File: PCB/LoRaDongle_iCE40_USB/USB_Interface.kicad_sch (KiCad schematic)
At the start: 28 parts, among them IC1 93LC56BT-I_OT, U2 FT232H, Y1 Crystal_GND24_Small

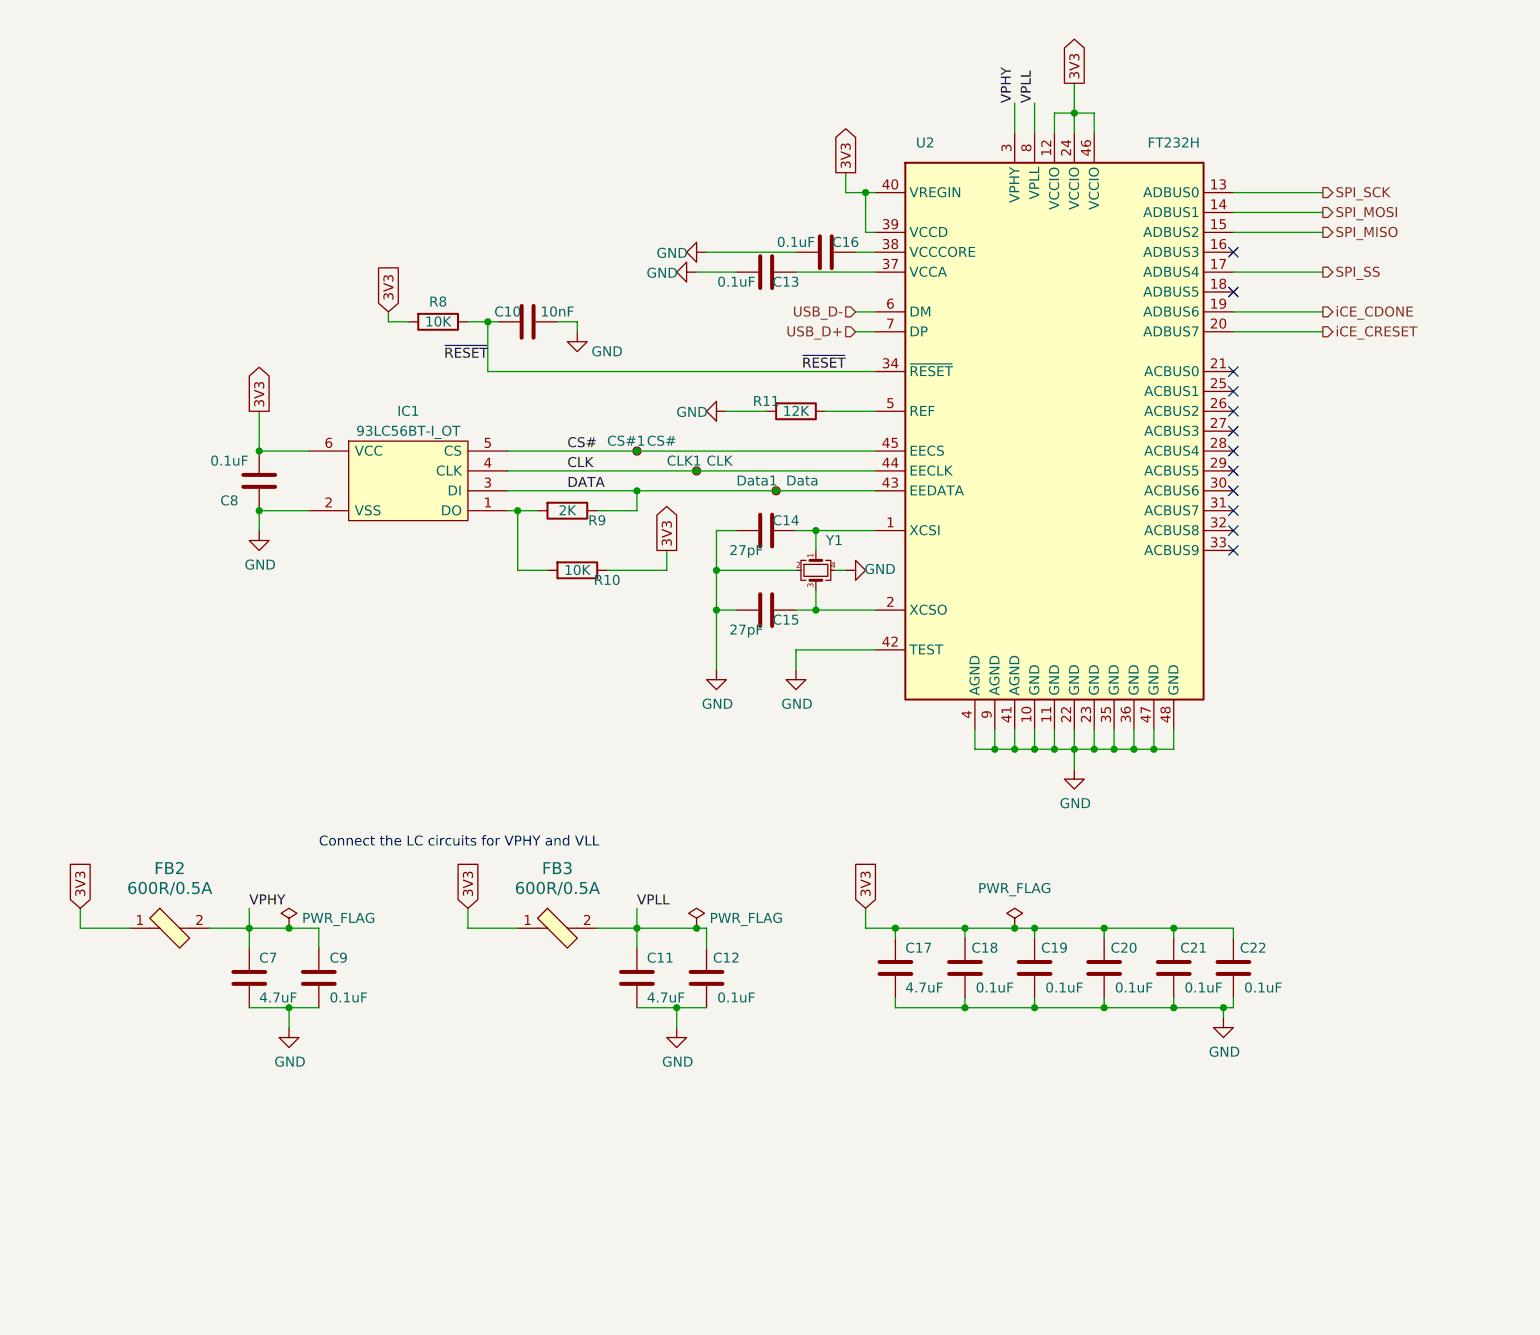
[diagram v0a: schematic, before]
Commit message: updated ftdi and flash chip, removed xilinx project
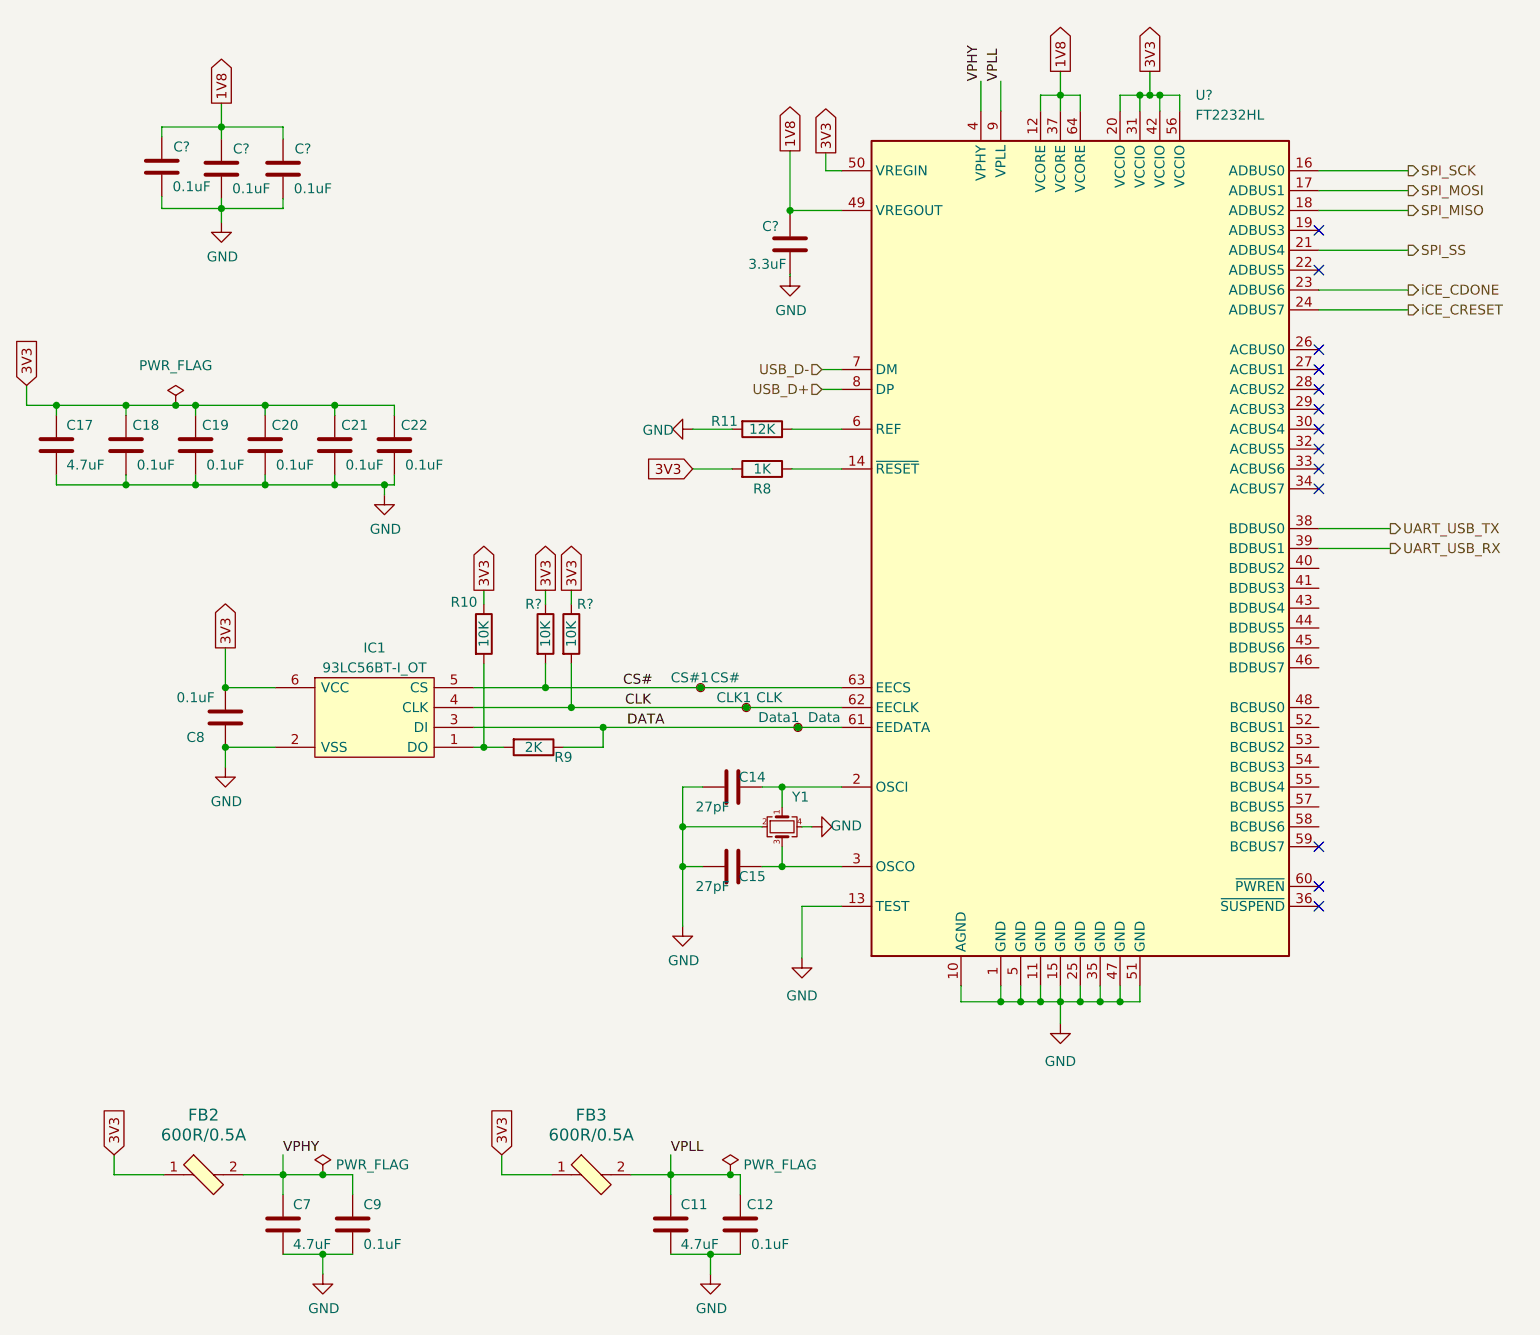
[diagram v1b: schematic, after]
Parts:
- removed C10: 10nF, Capacitor_SMD:C_0402_1005Metric_Pad0.74x0.62mm_HandSolder, symbol Device:C
- removed C13, C16: 0.1uF, Capacitor_SMD:C_0402_1005Metric_Pad0.74x0.62mm_HandSolder, symbol Device:C
- removed U2: FT232H, Package_QFP:LQFP-48_7x7mm_P0.5mm, symbol Interface_USB:FT232H
- added C? (x3): 0.1uF, Capacitor_SMD:C_0402_1005Metric_Pad0.74x0.62mm_HandSolder, symbol Device:C
- added C?: 3.3uF, symbol Device:C
- added R? (x2): 10K, Resistor_SMD:R_0402_1005Metric_Pad0.72x0.64mm_HandSolder, symbol Device:R
- added U?: FT2232HL, Package_QFP:LQFP-64_10x10mm_P0.5mm, symbol Interface_USB:FT2232HL
- R8: value 10K -> 1K; Manufacturer Part Number RMCF0402FT10K0 -> RMCF0402FT1K00
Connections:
- net 3V3: now also R?.1, R?.1, U?.20 (VCCIO), U?.31 (VCCIO), U?.42 (VCCIO), U?.50 (VREGIN), U?.56 (VCCIO)
- net CLK: now also R?.2, U?.62 (EECLK)
- net CS#: now also R?.2, U?.63 (EECS)
- net DATA: now also U?.61 (EEDATA)
- net GND: now also C?.1, C?.1, C?.1, C?.2, U?.1 (GND), U?.10 (AGND), U?.11 (GND), U?.13 (TEST), U?.15 (GND), U?.25 (GND), U?.35 (GND), U?.47 (GND), U?.5 (GND), U?.51 (GND)
- net SPI_MISO: now also U?.18 (ADBUS2)
- net SPI_MOSI: now also U?.17 (ADBUS1)
- net SPI_SCK: now also U?.16 (ADBUS0)
- net SPI_SS: now also U?.21 (ADBUS4)
- net USB_D+: now also U?.8 (DP)
- net USB_D-: now also U?.7 (DM)
- net VPHY: now also U?.4 (VPHY)
- net VPLL: now also U?.9 (VPLL)
- net iCE_CDONE: now also U?.23 (ADBUS6)
- net iCE_CRESET: now also U?.24 (ADBUS7)
- net at R11.1: now also U?.6 (REF)
- net at C14.1, Y1.1: now also U?.2 (OSCI)
- net at C15.1, Y1.3: now also U?.3 (OSCO)
- net ~{RESET}: no longer names the net of R8.1
- net ~{RESET}: now also U?.14 (~{RESET})
- new net 1V8: C?.1, C?.2, C?.2, C?.2, U?.12 (VCORE), U?.37 (VCORE), U?.49 (VREGOUT), U?.64 (VCORE)
- new net UART_USB_RX: U?.39 (BDBUS1)
- new net UART_USB_TX: U?.38 (BDBUS0)
- no-connect marks 12 -> 13
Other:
- note removed: "Connect the LC circuits for VPHY and VLL"
- moved on the sheet: C11, C12, C14, C15, C17, C18, C19, C20, C21, C22, C7, C8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

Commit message: updated jumpers, connectors and testpoints
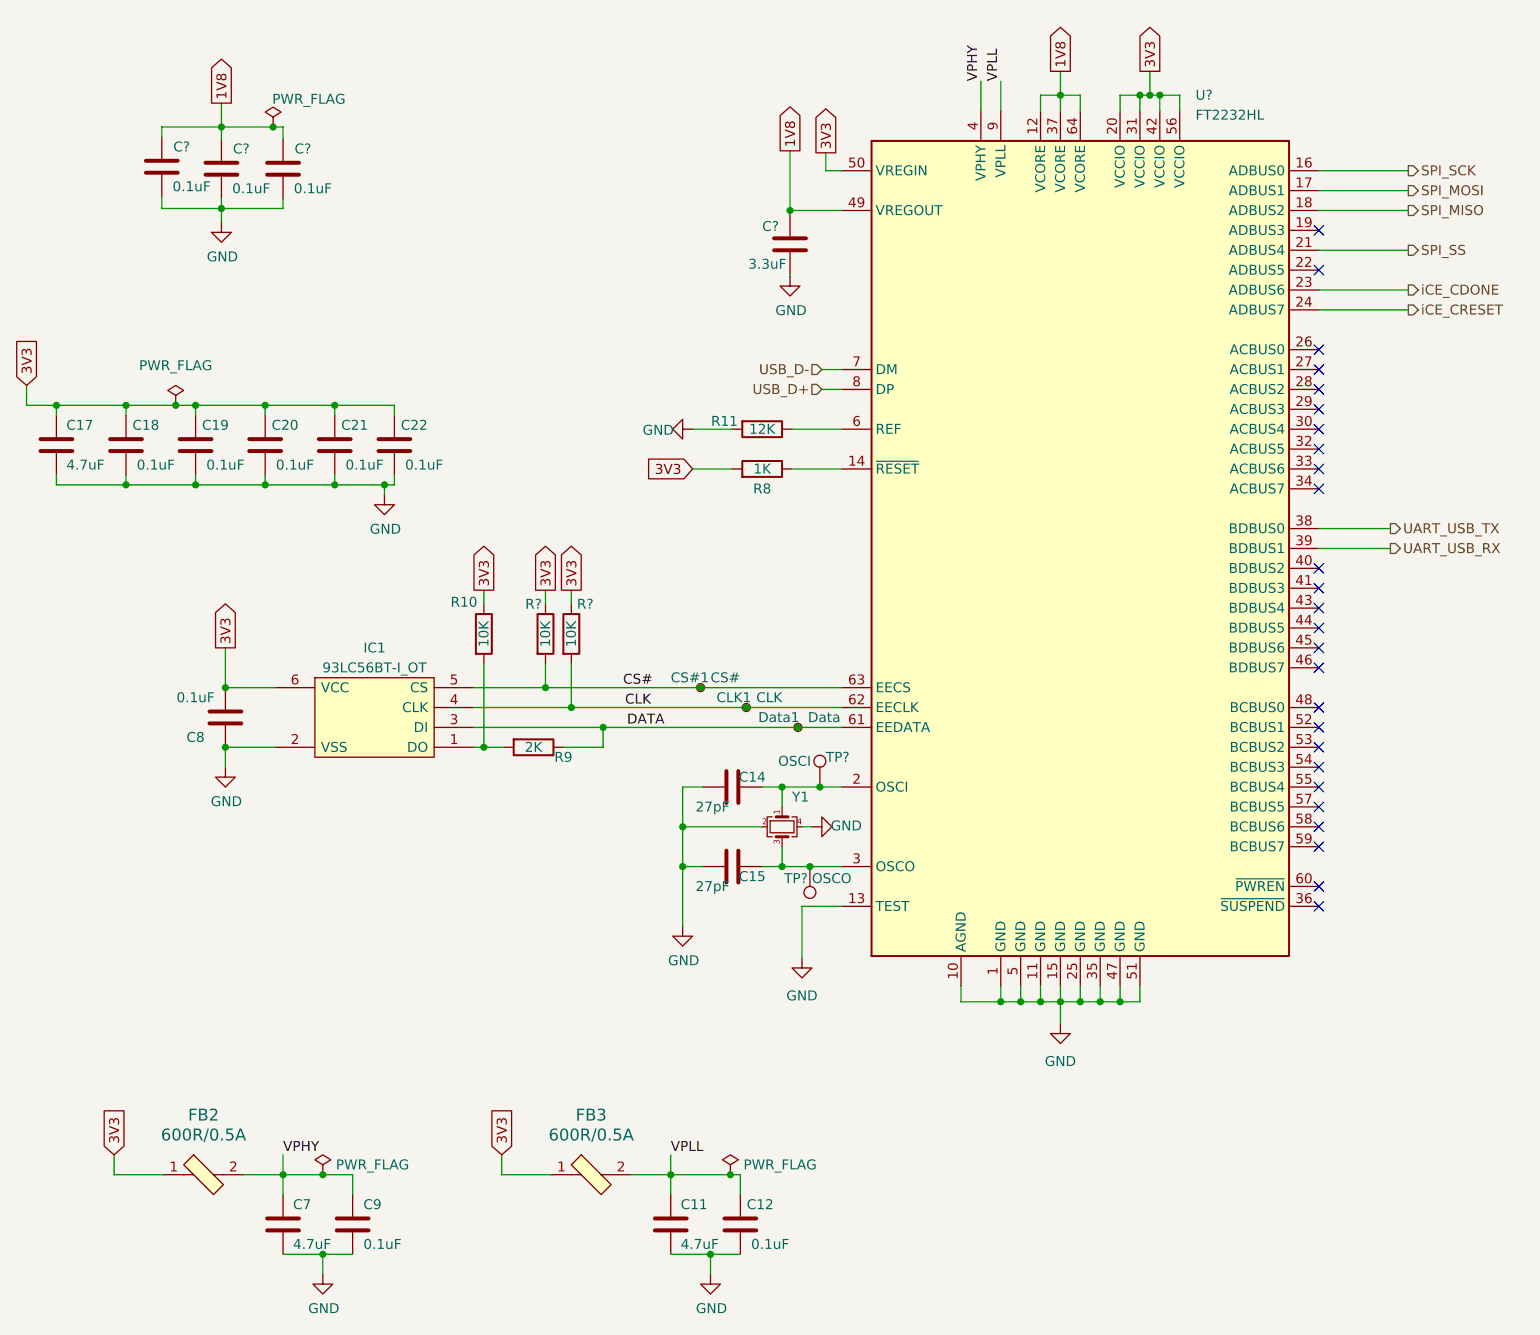
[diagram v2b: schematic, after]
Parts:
- added TP?: OSCO, symbol Connector:TestPoint
- added TP?: OSCI, symbol Connector:TestPoint
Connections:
- net at C15.1, U?.3 (OSCO), Y1.3: now also TP?.1
- net at C14.1, U?.2 (OSCI), Y1.1: now also TP?.1
- no-connect marks 13 -> 26
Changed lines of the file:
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@@
   (junction (at 54.102 67.818) (diameter 0) (color 0 0 0 0)
   )
+  (junction (at 66.548 32.258) (diameter 0) (color 0 0 0 0)
+  )
+  (junction (at 135.128 126.746) (diameter 0) (color 0 0 0 0)
+  )
   (junction (at 179.832 28.194) (diameter 0) (color 0 0 0 0)
   )
@@
   (junction (at 122.428 176.276) (diameter 0) (color 0 0 0 0)
   )
+  (junction (at 136.398 116.586) (diameter 0) (color 0 0 0 0)
+  )
   (junction (at 164.592 144.018) (diameter 0) (color 0 0 0 0)
   )
@@
   (junction (at 132.588 42.926) (diameter 0) (color 0 0 0 0)
   )
+  (no_connect (at 200.152 101.346))
+  (no_connect (at 200.152 114.046))
+  (no_connect (at 200.152 121.666))
   (no_connect (at 200.152 45.466))
+  (no_connect (at 200.152 106.426))
+  (no_connect (at 200.152 108.966))
+  (no_connect (at 200.152 98.806))
   (no_connect (at 200.152 131.826))
   (no_connect (at 200.152 129.286))
   (no_connect (at 200.152 124.206))
+  (no_connect (at 200.152 119.126))
   (no_connect (at 200.152 50.546))
   (no_connect (at 200.152 65.786))
@@
   (no_connect (at 200.152 70.866))
   (no_connect (at 200.152 78.486))
+  (no_connect (at 200.152 111.506))
+  (no_connect (at 200.152 116.586))
   (no_connect (at 200.152 60.706))
+  (no_connect (at 200.152 88.646))
+  (no_connect (at 200.152 91.186))
+  (no_connect (at 200.152 93.726))
+  (no_connect (at 200.152 96.266))
   (wire (pts (xy 74.422 77.978) (xy 80.772 77.978))
     (stroke (width 0) (type default) (color 0 0 0 0))
@@
     (stroke (width 0) (type default) (color 0 0 0 0))
   )
-  (wire (pts (xy 59.944 32.258) (xy 67.818 32.258))
+  (wire (pts (xy 59.944 32.258) (xy 66.548 32.258))
     (stroke (width 0) (type default) (color 0 0 0 0))
   )
@@
     (stroke (width 0) (type default) (color 0 0 0 0))
   )
-  (wire (pts (xy 139.192 126.746) (xy 131.572 126.746))
+  (wire (pts (xy 139.192 126.746) (xy 135.128 126.746))
     (stroke (width 0) (type default) (color 0 0 0 0))
   )
@@
     (stroke (width 0) (type default) (color 0 0 0 0))
   )
+  (wire (pts (xy 136.398 116.586) (xy 139.192 116.586))
+    (stroke (width 0) (type default) (color 0 0 0 0))
+  )
   (wire (pts (xy 169.672 28.194) (xy 169.672 30.226))
     (stroke (width 0) (type default) (color 0 0 0 0))
@@
     (stroke (width 0) (type default) (color 0 0 0 0))
   )
-  (wire (pts (xy 131.572 116.586) (xy 139.192 116.586))
+  (wire (pts (xy 131.572 116.586) (xy 136.398 116.586))
     (stroke (width 0) (type default) (color 0 0 0 0))
   )
@@
     (stroke (width 0) (type default) (color 0 0 0 0))
   )
+  (wire (pts (xy 66.548 32.258) (xy 67.818 32.258))
+    (stroke (width 0) (type default) (color 0 0 0 0))
+  )
   (wire (pts (xy 93.472 111.506) (xy 96.012 111.506))
     (stroke (width 0) (type default) (color 0 0 0 0))
@@
   )
   (wire (pts (xy 59.944 42.672) (xy 59.944 44.45))
+    (stroke (width 0) (type default) (color 0 0 0 0))
+  )
+  (wire (pts (xy 135.128 126.746) (xy 131.572 126.746))
     (stroke (width 0) (type default) (color 0 0 0 0))
   )
@@
   (symbol (lib_id "power:GND") (at 167.132 146.812 0) (unit 1)
     (in_bom yes) (on_board yes) (fields_autoplaced)
-    (property "Reference" "#PWR?" (id 0) (at 167.132 153.162 0)
+    (property "Reference" "#PWR0119" (id 0) (at 167.132 153.162 0)
       (effects (font (size 1.27 1.27)) hide)
     )
@@
   (symbol (lib_id "power:GND") (at 132.588 51.308 0) (unit 1)
     (in_bom yes) (on_board yes)
-    (property "Reference" "#PWR?" (id 0) (at 132.588 57.658 0)
+    (property "Reference" "#PWR0116" (id 0) (at 132.588 57.658 0)
       (effects (font (size 1.27 1.27)) hide)
     )
@@
   (symbol (lib_id "power:GND") (at 134.112 138.43 0) (unit 1)
     (in_bom yes) (on_board yes) (fields_autoplaced)
-    (property "Reference" "#PWR?" (id 0) (at 134.112 144.78 0)
+    (property "Reference" "#PWR0120" (id 0) (at 134.112 144.78 0)
       (effects (font (size 1.27 1.27)) hide)
     )
@@
     (pin "2")
   )
+  (symbol (lib_id "power:PWR_FLAG") (at 66.548 32.258 0) (unit 1)
+    (in_bom yes) (on_board yes)
+    (property "Reference" "#FLG0102" (id 0) (at 66.548 30.353 0)
+      (effects (font (size 1.27 1.27)) hide)
+    )
+    (property "Value" "PWR_FLAG" (id 1) (at 71.12 28.702 0))
+    (property "Footprint" "" (id 2) (at 66.548 32.258 0)
+      (effects (font (size 1.27 1.27)) hide)
+    )
+    (property "Datasheet" "~" (id 3) (at 66.548 32.258 0)
+      (effects (font (size 1.27 1.27)) hide)
+    )
+    (pin "1")
+  )
+  (symbol (lib_id "Connector:TestPoint") (at 135.128 126.746 180) (unit 1)
+    (in_bom yes) (on_board yes)
+    (property "Reference" "TP?" (id 0) (at 131.826 128.27 0)
+      (effects (font (size 1.27 1.27)) (justify right))
+    )
+    (property "Value" "OSCO" (id 1) (at 135.382 128.27 0)
+      (effects (font (size 1.27 1.27)) (justify right))
+    )
+    (property "Footprint" "" (id 2) (at 130.048 126.746 0)
+      (effects (font (size 1.27 1.27)) hide)
+    )
+    (property "Datasheet" "~" (id 3) (at 130.048 126.746 0)
+      (effects (font (size 1.27 1.27)) hide)
+    )
+    (pin "1")
+  )
   (symbol (lib_id "power:GND") (at 59.944 44.45 0) (unit 1)
     (in_bom yes) (on_board yes)
-    (property "Reference" "#PWR?" (id 0) (at 59.944 50.8 0)
+    (property "Reference" "#PWR0115" (id 0) (at 59.944 50.8 0)
       (effects (font (size 1.27 1.27)) hide)
     )
@@
       (effects (font (size 1.27 1.27)) hide)
     )
+    (pin "1")
+  )
+  (symbol (lib_id "Connector:TestPoint") (at 136.398 116.586 0) (unit 1)
+    (in_bom yes) (on_board yes)
+    (property "Reference" "TP?" (id 0) (at 137.16 112.776 0)
+      (effects (font (size 1.27 1.27)) (justify left))
+    )
+    (property "Value" "OSCI" (id 1) (at 131.064 113.284 0)
+      (effects (font (size 1.27 1.27)) (justify left))
+    )
+    (property "Footprint" "" (id 2) (at 141.478 116.586 0)
+      (effects (font (size 1.27 1.27)) hide)
+    )
+    (property "Datasheet" "~" (id 3) (at 141.478 116.586 0)
+      (effects (font (size 1.27 1.27)) hide)
+    )

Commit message: updated layout and routing
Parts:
- removed CLK1: CLK, TestPoint:TestPoint_Pad_D1.0mm, symbol Connector:TestPoint_Small
- removed CS#1: CS#, TestPoint:TestPoint_Pad_D1.0mm, symbol Connector:TestPoint_Small
- removed Data1: Data, TestPoint:TestPoint_Pad_D1.0mm, symbol Connector:TestPoint_Small
- added J7: Conn_01x03_Male, Connector_PinHeader_2.54mm:PinHeader_1x03_P2.54mm_Vertical, symbol Connector:Conn_01x03_Male
- C53: renamed from C?; footprint (none) -> Capacitor_SMD:C_0603_1608Metric_Pad1.08x0.95mm_HandSolder; Manufacturer (none) -> Samsung Electro-Mechanics; Manufacturer Part Number (none) -> CL10A335KP8NNNC; Package (none) -> 0603; Type (none) -> SMD
- OSCI1, OSCO1: renamed from TP?; footprint (none) -> TestPoint:TestPoint_Pad_D2.5mm; Manufacturer (none) -> -; Manufacturer Part Number (none) -> -; Package (none) -> -
- U2: renamed from U?; Manufacturer (none) -> FTDI, Future Technology Devices International Ltd; Manufacturer Part Number (none) -> FT2232HL; Package (none) -> 64-LQFP
- gave numbers to parts that had none: 5
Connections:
- net CLK: now also J7.2 (Pin_2)
- net CS#: no longer IC1.5 (CS), R22.2, U2.63 (EECS)
- net DATA: now also J7.1 (Pin_1)
- new net: IC1.5 (CS), J7.3 (Pin_3), R22.2, U2.63 (EECS)

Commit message: updated routing
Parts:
- J7: Manufacturer (none) -> -; Manufacturer Part Number (none) -> -; Package (none) -> -
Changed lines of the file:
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@@
+      (effects (font (size 1.27 1.27)) hide)
+    )
+    (property "Description" "1x03 Male Header" (id 4) (at 123.444 90.932 0)
+      (effects (font (size 1.27 1.27)) hide)
+    )
+    (property "Manufacturer" "-" (id 5) (at 123.444 90.932 0)
+      (effects (font (size 1.27 1.27)) hide)
+    )
+    (property "Manufacturer Part Number" "-" (id 6) (at 123.444 90.932 0)
+      (effects (font (size 1.27 1.27)) hide)
+    )
+    (property "Package" "-" (id 7) (at 123.444 90.932 0)
       (effects (font (size 1.27 1.27)) hide)
     )
